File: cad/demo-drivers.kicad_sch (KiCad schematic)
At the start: 45 parts, among them Q1 Q_PNP_EBC, Q2 Q_PNP_EBC, Q3 Q_PNP_EBC, Q4 Q_PNP_EBC, SW1 SW_Push, U1 SHTC3, U2 DS3231MZ, U3 AT24CS02-SSHM, U4 MCP23S08-xP, U5 MCP23008-xP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

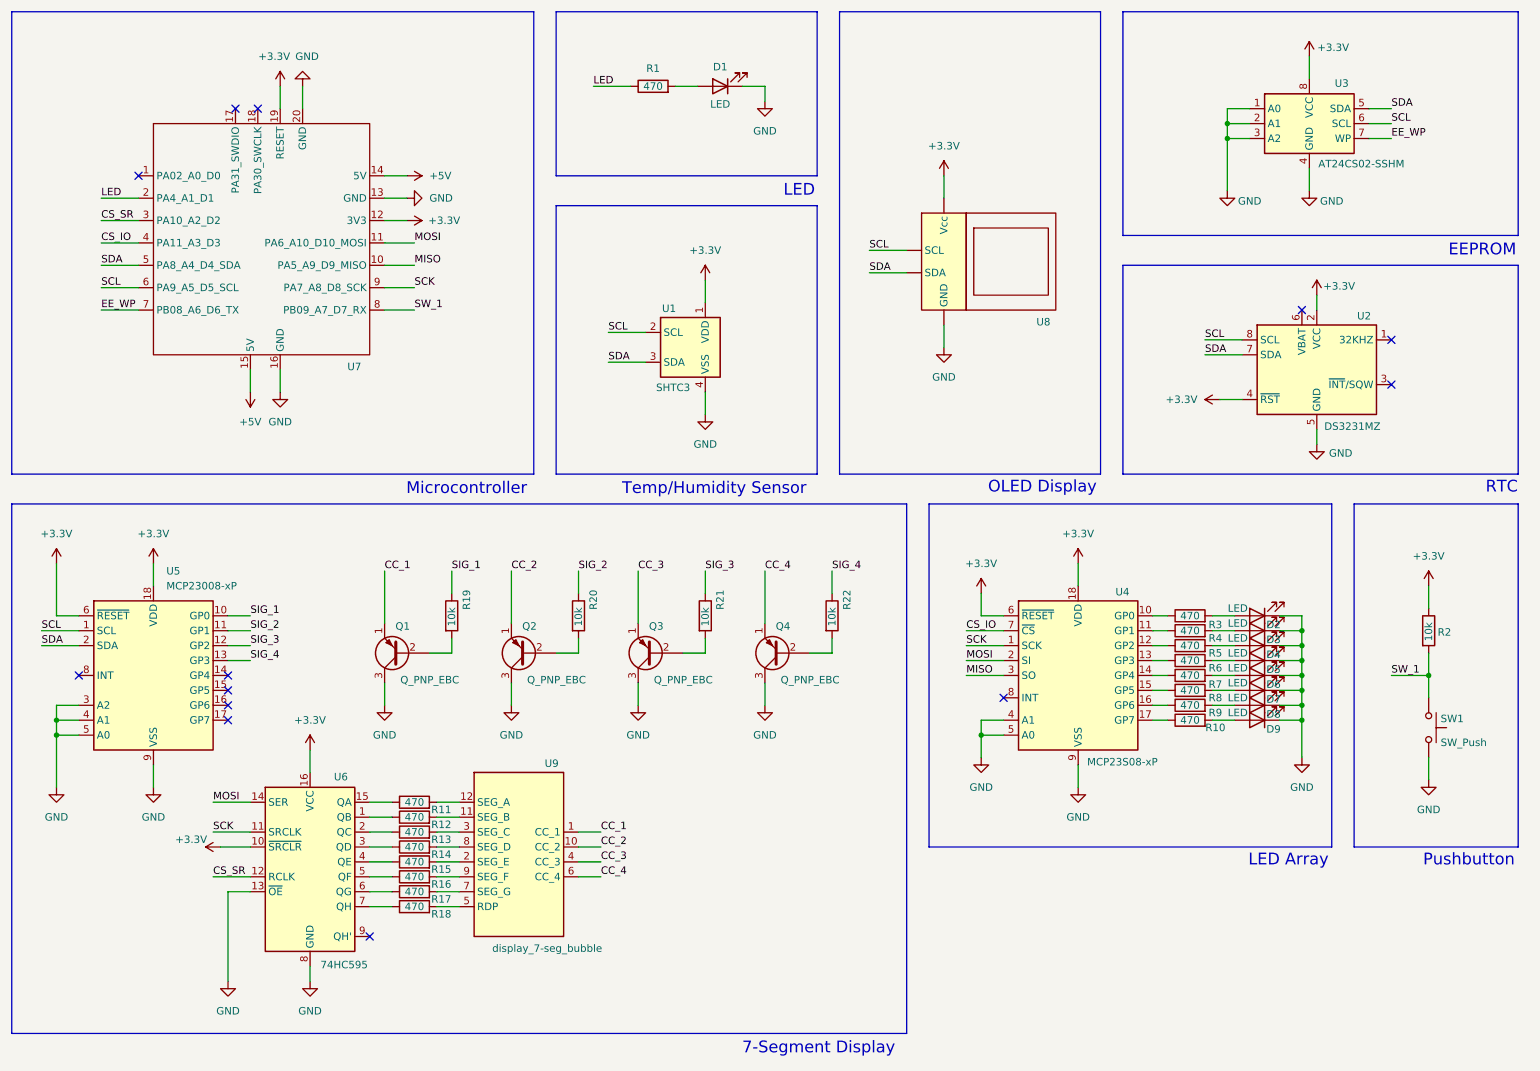
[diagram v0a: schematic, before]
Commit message: Update schematic labels
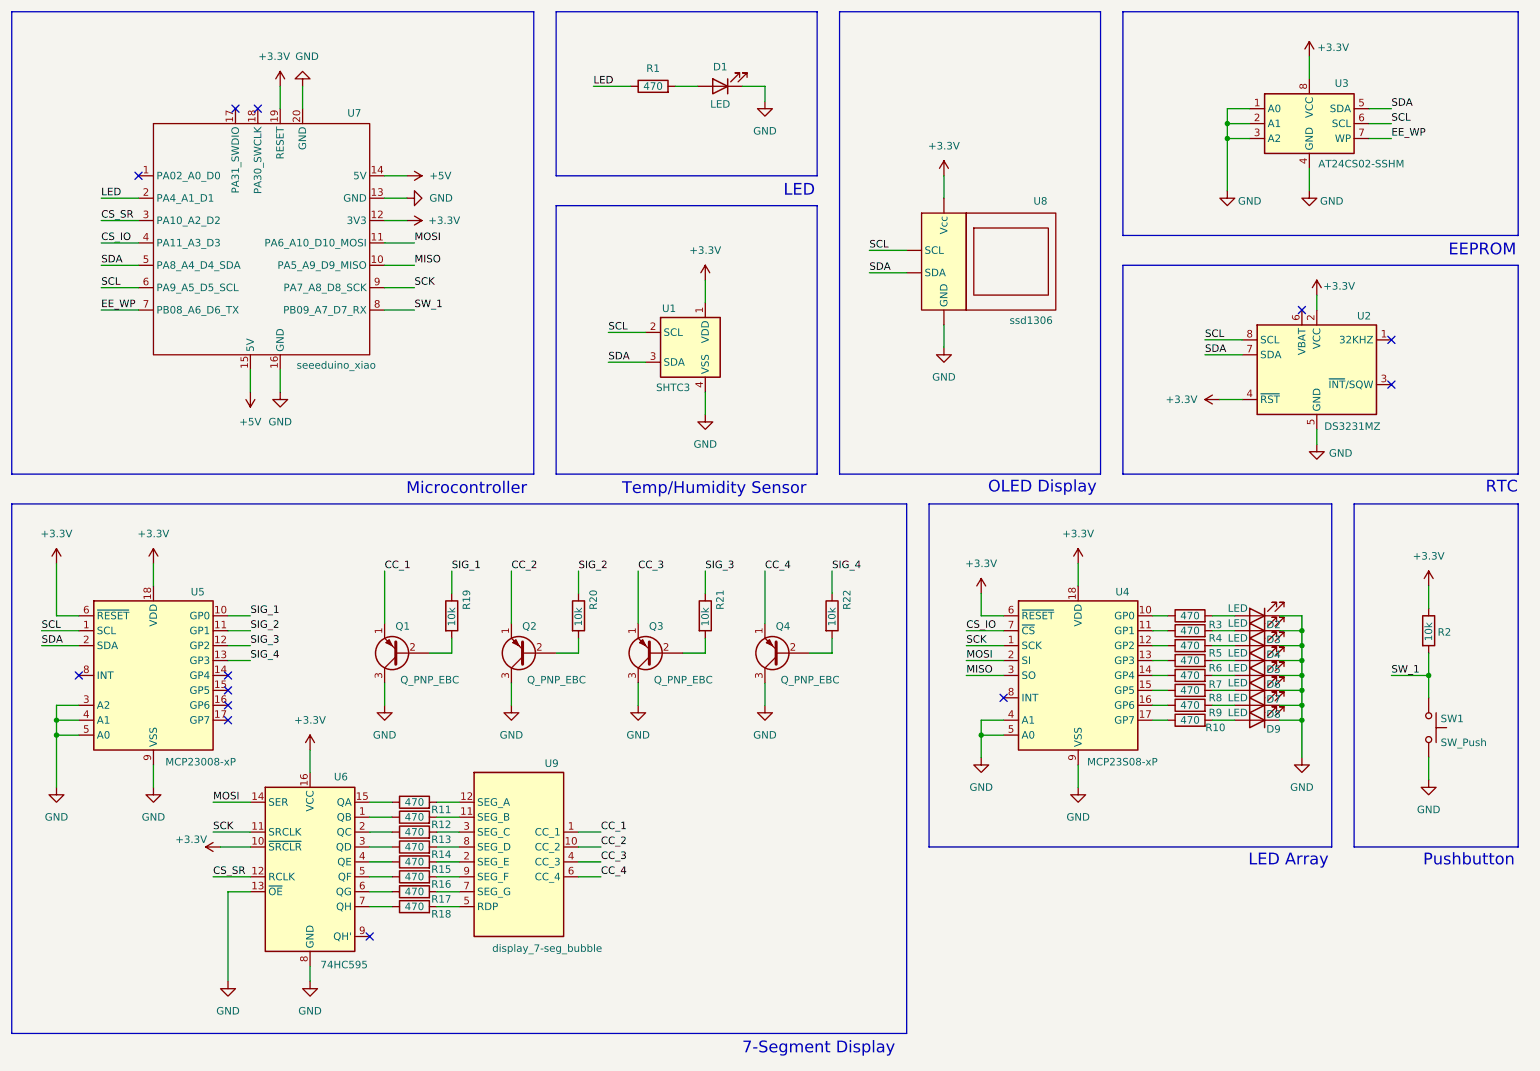
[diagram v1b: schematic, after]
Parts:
- U7: value ~ -> seeeduino_xiao
- U8: value ~ -> ssd1306
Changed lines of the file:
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@@
 		(on_board yes)
 		(dnp no)
-		(fields_autoplaced yes)
 		(property "Reference" "U5"
-			(at 46.6441 113.03 0)
+			(at 50.8 116.586 0)
 			(effects
 				(font
@@
 		)
 		(property "Value" "MCP23008-xP"
-			(at 46.6441 115.57 0)
+			(at 46.482 145.542 0)
 			(effects
 				(font
@@
 		(dnp no)
 		(property "Reference" "U7"
-			(at 77.47 78.232 0)
+			(at 77.47 35.052 0)
 			(effects
 				(font
@@
 			)
 		)
-		(property "Value" "~"
-			(at 68.2341 80.01 0)
+		(property "Value" "seeeduino_xiao"
+			(at 68.834 77.978 0)
 			(effects
 				(font
@@
 		(dnp no)
 		(property "Reference" "U8"
-			(at 194.818 70.612 0)
+			(at 194.31 50.038 0)
 			(effects
 				(font
@@
 			)
 		)
-		(property "Value" "~"
-			(at 199.39 61.595 0)
+		(property "Value" "ssd1306"
+			(at 190.246 70.358 0)
 			(effects
 				(font

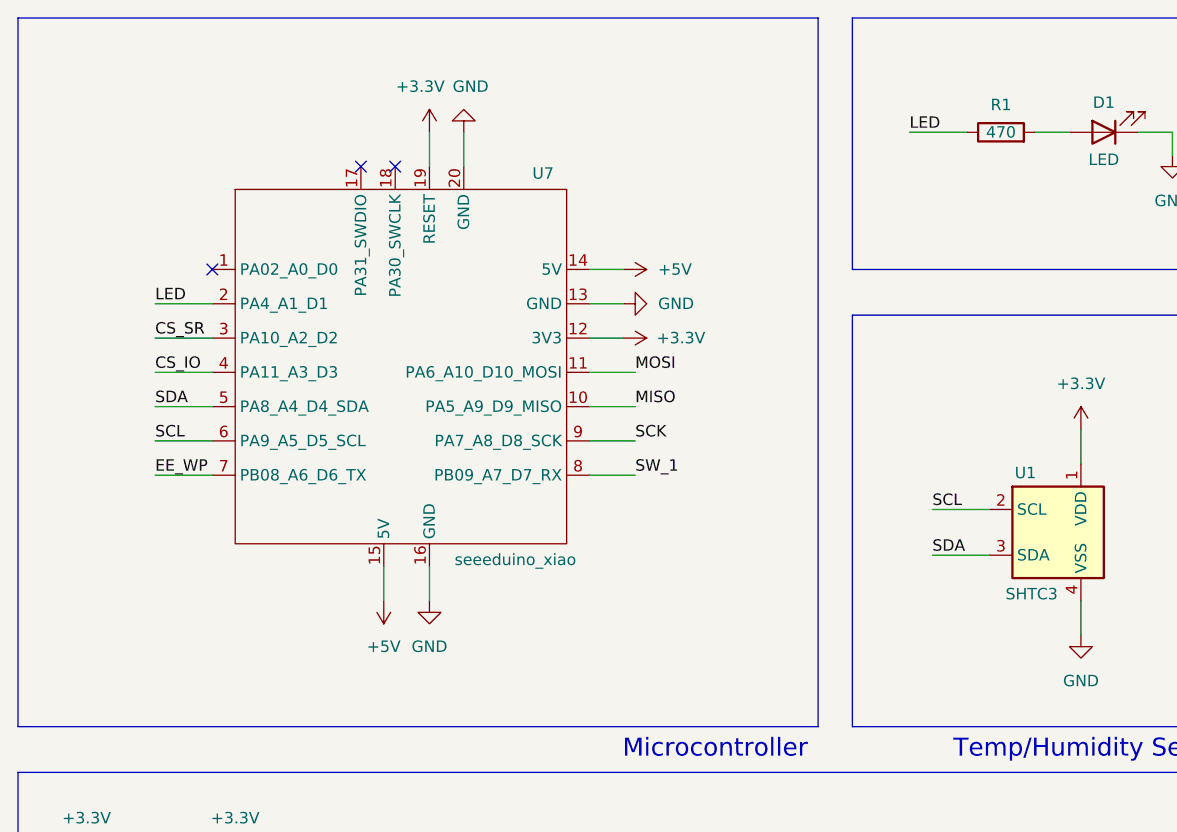
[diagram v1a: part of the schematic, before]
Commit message: Add i2c bus pull-up resistors to schematic
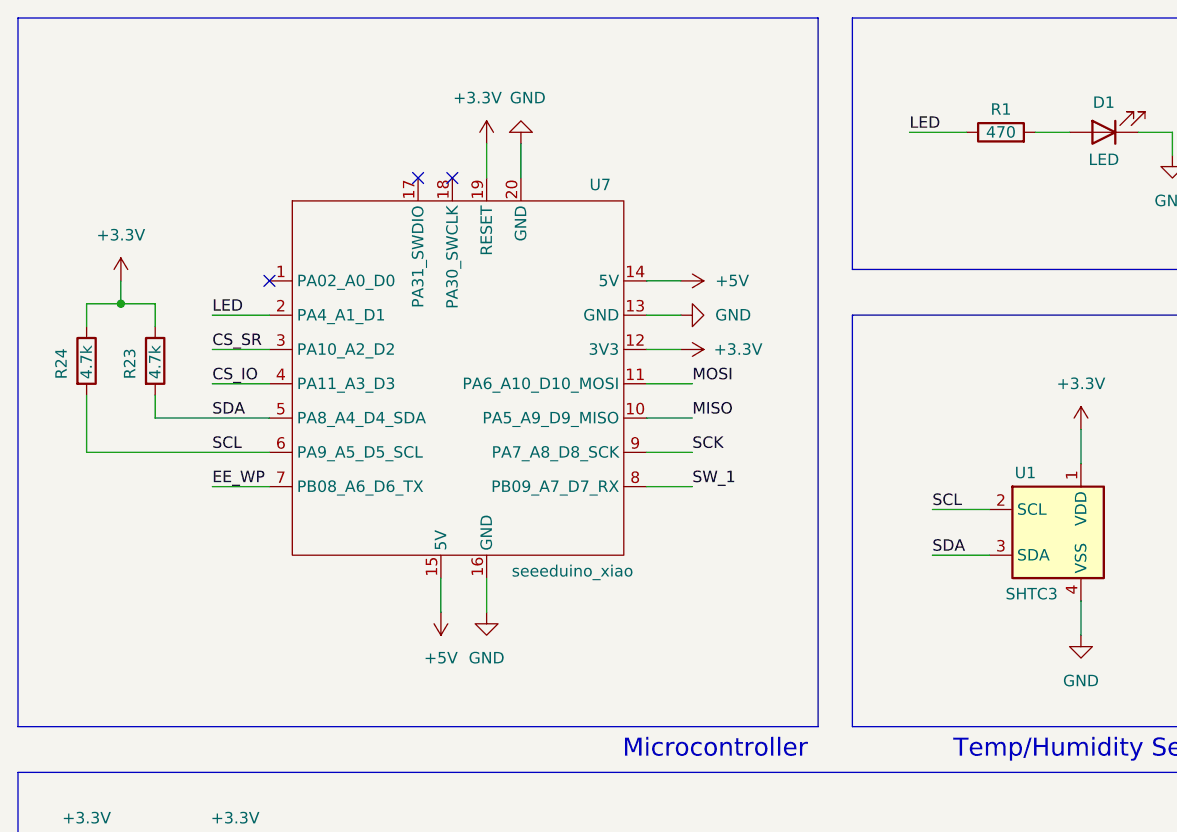
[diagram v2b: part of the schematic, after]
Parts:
- added R23, R24: 4.7k, symbol Device:R
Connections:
- net +3.3V: now also R23.1, R24.1
- net SCL: now also R24.2
- net SDA: now also R23.2
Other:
- moved on the sheet: U7
